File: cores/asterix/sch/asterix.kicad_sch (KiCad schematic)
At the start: 1 part

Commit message: sound and pcm done! wip objects
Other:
- sheet colmix ports: added ~{SYSRES}; removed ~{RESET}
- sheet pcm ports: added ~{SYSRES}; removed ~{RESET}
- sheet scroll ports: added ~{SYSRES}; removed ~{RESET}
- sheet sound ports: added PCMCLK, PCM~{CS}, STBI, ~{SYSRES}; removed SC~{CS}, SH2, SO~{CLK}, S~{CLK}, ~{RESET}
- note added: "OK"
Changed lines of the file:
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@@
-    (stroke (width 0) (type default))
-  )
-  (wire (pts (xy 203.2 57.15) (xy 219.71 57.15))
     (stroke (width 0) (type default))
   )
@@
     (stroke (width 0) (type default))
   )
-  (wire (pts (xy 219.71 54.61) (xy 203.2 54.61))
-    (stroke (width 0) (type default))
-  )
   (wire (pts (xy 148.59 92.71) (xy 165.1 92.71))
     (stroke (width 0) (type default))
@@
     (stroke (width 0) (type default))
   )
-  (wire (pts (xy 203.2 59.69) (xy 219.71 59.69))
+  (wire (pts (xy 203.2 54.61) (xy 219.71 54.61))
     (stroke (width 0) (type default))
   )
@@
   )
   (wire (pts (xy 39.37 107.95) (xy 50.8 107.95))
+    (stroke (width 0) (type default))
+  )
+  (wire (pts (xy 148.59 44.45) (xy 165.1 44.45))
     (stroke (width 0) (type default))
   )
@@
     )
   )
+  (text "OK" (at 184.15 109.22 0)
+    (effects (font (size 1.27 1.27)) (justify left bottom))
+  )
   (text "VSS" (at 39.37 100.33 0)
     (effects (font (size 1.27 1.27)) (justify left bottom))
   )
+  (text "OK" (at 176.53 52.07 0)
+    (effects (font (size 1.27 1.27)) (justify left bottom))
+  )
   (text "VSS" (at 97.79 102.87 0)
     (effects (font (size 1.27 1.27)) (justify left bottom))
@@
     (effects (font (size 1.27 1.27)) (justify left bottom))
   )
-  (label "SC~{CS}" (at 219.71 39.37 180) (fields_autoplaced)
+  (label "PCM~{CS}" (at 219.71 39.37 180) (fields_autoplaced)
     (effects (font (size 1.27 1.27)) (justify right bottom))
   )
@@
     (effects (font (size 1.27 1.27)) (justify right bottom))
   )
+  (label "SH1" (at 148.59 44.45 0) (fields_autoplaced)
+    (effects (font (size 1.27 1.27)) (justify left bottom))
+  )
   (label "COIN_1" (at 39.37 118.11 0) (fields_autoplaced)
     (effects (font (size 1.27 1.27)) (justify left bottom))
@@
     (effects (font (size 1.27 1.27)) (justify left bottom))
   )
-  (label "~{RESET}" (at 311.15 207.01 0) (fields_autoplaced)
+  (label "~{SYSRES}" (at 311.15 207.01 0) (fields_autoplaced)
     (effects (font (size 1.27 1.27)) (justify left bottom))
   )
@@
     (effects (font (size 1.27 1.27)) (justify left bottom))
   )
-  (label "~{RESET}" (at 148.59 41.91 0) (fields_autoplaced)
+  (label "~{SYSRES}" (at 148.59 41.91 0) (fields_autoplaced)
     (effects (font (size 1.27 1.27)) (justify left bottom))
   )
@@
     (effects (font (size 1.27 1.27)) (justify right bottom))
   )
-  (label "SH1" (at 219.71 44.45 180) (fields_autoplaced)
+  (label "STBI" (at 219.71 44.45 180) (fields_autoplaced)
     (effects (font (size 1.27 1.27)) (justify right bottom))
   )
@@
     (effects (font (size 1.27 1.27)) (justify right bottom))
   )
-  (label "~{RESET}" (at 382.27 130.81 180) (fields_autoplaced)
+  (label "~{SYSRES}" (at 382.27 130.81 180) (fields_autoplaced)
     (effects (font (size 1.27 1.27)) (justify right bottom))
   )
@@
     (effects (font (size 1.27 1.27)) (justify left bottom))
   )
-  (label "~{RESET}" (at 148.59 115.57 0) (fields_autoplaced)
+  (label "~{SYSRES}" (at 148.59 115.57 0) (fields_autoplaced)
     (effects (font (size 1.27 1.27)) (justify left bottom))
   )
@@
     (effects (font (size 1.27 1.27)) (justify left bottom))
   )
-  (label "SO~{CLK}" (at 219.71 54.61 180) (fields_autoplaced)
-    (effects (font (size 1.27 1.27)) (justify right bottom))
-  )
   (label "IOCS" (at 148.59 189.23 0) (fields_autoplaced)
     (effects (font (size 1.27 1.27)) (justify left bottom))
@@
     (effects (font (size 1.27 1.27)) (justify right bottom))
   )
+  (label "PCMCLK" (at 148.59 118.11 0) (fields_autoplaced)
+    (effects (font (size 1.27 1.27)) (justify left bottom))
+  )
   (label "2P_BTN_4" (at 97.79 140.97 180) (fields_autoplaced)
     (effects (font (size 1.27 1.27)) (justify right bottom))
@@
     (effects (font (size 1.27 1.27)) (justify left bottom))
   )
-  (label "SH2" (at 219.71 46.99 180) (fields_autoplaced)
-    (effects (font (size 1.27 1.27)) (justify right bottom))
-  )
   (label "OBJPXL[8..0]" (at 381 41.91 180) (fields_autoplaced)
     (effects (font (size 1.27 1.27)) (justify right bottom))
@@
     (effects (font (size 1.27 1.27)) (justify left bottom))
   )
-  (label "S~{RD}" (at 219.71 59.69 180) (fields_autoplaced)
+  (label "S~{RD}" (at 219.71 54.61 180) (fields_autoplaced)
     (effects (font (size 1.27 1.27)) (justify right bottom))
   )
@@
     (effects (font (size 1.27 1.27)) (justify left bottom))
   )
+  (label "PCMCLK" (at 219.71 46.99 180) (fields_autoplaced)
+    (effects (font (size 1.27 1.27)) (justify right bottom))
+  )
   (label "MAIN_DB[7..0]" (at 300.99 125.73 180) (fields_autoplaced)
     (effects (font (size 1.27 1.27)) (justify right bottom))
@@
     (effects (font (size 1.27 1.27)) (justify left bottom))
   )
-  (label "S~{CLK}" (at 219.71 57.15 180) (fields_autoplaced)
-    (effects (font (size 1.27 1.27)) (justify right bottom))
-  )
   (label "MAIN_A0" (at 300.99 130.81 180) (fields_autoplaced)
     (effects (font (size 1.27 1.27)) (justify right bottom))
@@
   (label "~{HBLANK}" (at 382.27 120.65 180) (fields_autoplaced)
     (effects (font (size 1.27 1.27)) (justify right bottom))
-  )
-  (label "S~{CLK}" (at 148.59 118.11 0) (fields_autoplaced)
-    (effects (font (size 1.27 1.27)) (justify left bottom))
   )
   (label "2P_START" (at 148.59 227.33 0) (fields_autoplaced)
@@
       (effects (font (size 1.27 1.27)) (justify left))
     )
-    (pin "~{RESET}" output (at 365.76 130.81 0)
+    (pin "~{SYSRES}" output (at 365.76 130.81 0)
       (effects (font (size 1.27 1.27)) (justify right))
     )
@@
       (effects (font (size 1.27 1.27)) (justify left))
     )
-    (pin "~{RESET}" input (at 327.66 207.01 180)
+    (pin "~{SYSRES}" input (at 327.66 207.01 180)
       (effects (font (size 1.27 1.27)) (justify left))
     )
@@
       (effects (font (size 1.27 1.27)) (justify left))
     )
-    (pin "~{RESET}" input (at 165.1 115.57 180)
+    (pin "~{SYSRES}" input (at 165.1 115.57 180)
       (effects (font (size 1.27 1.27)) (justify left))
     )
@@
       (effects (font (size 1.27 1.27)) (justify left top))
     )
-    (pin "SC~{CS}" output (at 203.2 39.37 0)
+    (pin "PCMCLK" output (at 203.2 46.99 0)
+      (effects (font (size 1.27 1.27)) (justify right))
+    )
+    (pin "S~{RD}" output (at 203.2 54.61 0)
+      (effects (font (size 1.27 1.27)) (justify right))
+    )
+    (pin "~{SOUND}" input (at 165.1 39.37 180)
+      (effects (font (size 1.27 1.27)) (justify left))
+    )
+    (pin "SH1" input (at 165.1 44.45 180)
+      (effects (font (size 1.27 1.27)) (justify left))
+    )
+    (pin "~{SYSRES}" input (at 165.1 41.91 180)
+      (effects (font (size 1.27 1.27)) (justify left))
+    )
+    (pin "SND_A[15..0]" output (at 203.2 52.07 0)
+      (effects (font (size 1.27 1.27)) (justify right))
+    )
+    (pin "SND_D[7..0]" tri_state (at 203.2 49.53 0)
       (effects (font (size 1.27 1.27)) (justify right))
     )
@@
       (effects (font (size 1.27 1.27)) (justify right))
     )
-    (pin "SH1" output (at 203.2 44.45 0)
-      (effects (font (size 1.27 1.27)) (justify right))
-    )
-    (pin "SH2" output (at 203.2 46.99 0)
-      (effects (font (size 1.27 1.27)) (justify right))
-    )
-    (pin "SND_D[7..0]" tri_state (at 203.2 49.53 0)
-      (effects (font (size 1.27 1.27)) (justify right))
-    )
-    (pin "SND_A[15..0]" output (at 203.2 52.07 0)
-      (effects (font (size 1.27 1.27)) (justify right))
-    )
-    (pin "~{SOUND}" input (at 165.1 39.37 180)
-      (effects (font (size 1.27 1.27)) (justify left))
-    )
-    (pin "~{RESET}" input (at 165.1 41.91 180)
-      (effects (font (size 1.27 1.27)) (justify left))
-    )
-    (pin "S~{CLK}" output (at 203.2 57.15 0)
-      (effects (font (size 1.27 1.27)) (justify right))
-    )
-    (pin "S~{RD}" output (at 203.2 59.69 0)
-      (effects (font (size 1.27 1.27)) (justify right))
-    )
-    (pin "SO~{CLK}" output (at 203.2 54.61 0)
-      (effects (font (size 1.27 1.27)) (justify right))
-    )
+    (pin "STBI" output (at 203.2 44.45 0)
+      (effects (font (size 1.27 1.27)) (justify right))
+    )
+    (pin "PCM~{CS}" output (at 203.2 39.37 0)
+      (effects (font (size 1.27 1.27)) (justify right))
+    )

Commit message: wip obj asterix
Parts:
- gave numbers to parts that had none: 1
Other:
- sheet pcm ports: added MAIN_A1, MAIN_D[7..0], PCMCLK, PCM~{CS}, STBI; removed MAIN_A0, MAIN_DB[7..0], SC~{CS}, SH2, SO~{CLK}, S~{CLK}
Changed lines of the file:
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@@
     (stroke (width 0) (type default))
   )
-  (wire (pts (xy 148.59 123.19) (xy 165.1 123.19))
+  (wire (pts (xy 148.59 100.33) (xy 165.1 100.33))
     (stroke (width 0) (type default))
   )
@@
     (stroke (width 0) (type default))
   )
-  (wire (pts (xy 148.59 120.65) (xy 165.1 120.65))
-    (stroke (width 0) (type default))
-  )
   (wire (pts (xy 92.71 81.28) (xy 92.71 83.82))
     (stroke (width 0) (type default))
@@
     (stroke (width 0) (type default))
   )
-  (wire (pts (xy 148.59 100.33) (xy 165.1 100.33))
+  (wire (pts (xy 219.71 102.87) (xy 203.2 102.87))
     (stroke (width 0) (type default))
   )
@@
     (effects (font (size 1.27 1.27)) (justify right bottom))
   )
-  (label "SC~{CS}" (at 148.59 120.65 0) (fields_autoplaced)
-    (effects (font (size 1.27 1.27)) (justify left bottom))
-  )
   (label "~{VSYNC}" (at 311.15 44.45 0) (fields_autoplaced)
     (effects (font (size 1.27 1.27)) (justify left bottom))
@@
     (effects (font (size 1.27 1.27)) (justify left bottom))
   )
-  (label "SH1" (at 148.59 100.33 0) (fields_autoplaced)
-    (effects (font (size 1.27 1.27)) (justify left bottom))
+  (label "SH1" (at 219.71 102.87 180) (fields_autoplaced)
+    (effects (font (size 1.27 1.27)) (justify right bottom))
   )
   (label "1P_DOWN" (at 148.59 199.39 0) (fields_autoplaced)
@@
     (effects (font (size 1.27 1.27)) (justify right bottom))
   )
-  (label "SH2" (at 148.59 102.87 0) (fields_autoplaced)
+  (label "STBI" (at 148.59 102.87 0) (fields_autoplaced)
     (effects (font (size 1.27 1.27)) (justify left bottom))
   )
@@
     (effects (font (size 1.27 1.27)) (justify left bottom))
   )
-  (label "MAIN_A0" (at 148.59 105.41 0) (fields_autoplaced)
+  (label "MAIN_A1" (at 148.59 105.41 0) (fields_autoplaced)
     (effects (font (size 1.27 1.27)) (justify left bottom))
   )
@@
     (effects (font (size 1.27 1.27)) (justify right bottom))
   )
-  (label "SO~{CLK}" (at 148.59 123.19 0) (fields_autoplaced)
+  (label "PCM~{CS}" (at 148.59 100.33 0) (fields_autoplaced)
     (effects (font (size 1.27 1.27)) (justify left bottom))
   )
@@
   (symbol (lib_id "arcade:JAMMA_CONN") (at 54.61 78.74 0) (unit 1)
     (in_bom yes) (on_board yes) (dnp no)
-    (property "Reference" "JM?" (at 68.58 88.9 0)
+    (property "Reference" "JM1" (at 68.58 88.9 0)
       (effects (font (size 3.5052 3.5052)))
     )
@@
       (project "asterix"
         (path "/0011ec10-82c4-4039-b424-337480f568e8"
-          (reference "JM?") (unit 1)
+          (reference "JM1") (unit 1)
         )
       )
@@
     )
   )
-  (sheet (at 165.1 90.17) (size 38.1 35.56) (fields_autoplaced)
+  (sheet (at 165.1 90.17) (size 38.1 30.48) (fields_autoplaced)
     (stroke (width 0.1524) (type solid))
     (fill (color 0 0 0 0.0000))
@@
       (effects (font (size 1.27 1.27)) (justify left bottom))
     )
-    (property "Sheetfile" "pcm.kicad_sch" (at 165.1 126.3146 0)
+    (property "Sheetfile" "pcm.kicad_sch" (at 165.1 121.2346 0)
       (effects (font (size 1.27 1.27)) (justify left top))
     )
-    (pin "SH2" input (at 165.1 102.87 180)
+    (pin "~{MCS}" input (at 165.1 107.95 180)
+      (effects (font (size 1.27 1.27)) (justify left))
+    )
+    (pin "MAIN_A1" input (at 165.1 105.41 180)
+      (effects (font (size 1.27 1.27)) (justify left))
+    )
+    (pin "S~{RD}" input (at 165.1 110.49 180)
+      (effects (font (size 1.27 1.27)) (justify left))
+    )
+    (pin "SH1" output (at 203.2 102.87 0)
+      (effects (font (size 1.27 1.27)) (justify right))
+    )
+    (pin "MAIN_D[7..0]" bidirectional (at 203.2 95.25 0)
+      (effects (font (size 1.27 1.27)) (justify right))
+    )
+    (pin "SND_D[7..0]" bidirectional (at 203.2 92.71 0)
+      (effects (font (size 1.27 1.27)) (justify right))
+    )
+    (pin "PCMCLK" input (at 165.1 118.11 180)
       (effects (font (size 1.27 1.27)) (justify left))
     )
@@
       (effects (font (size 1.27 1.27)) (justify left))
     )
-    (pin "SH1" input (at 165.1 100.33 180)
+    (pin "PCM~{CS}" input (at 165.1 100.33 180)
+      (effects (font (size 1.27 1.27)) (justify left))
+    )
+    (pin "AUX1" input (at 165.1 95.25 180)
+      (effects (font (size 1.27 1.27)) (justify left))
+    )
+    (pin "STBI" input (at 165.1 102.87 180)
+      (effects (font (size 1.27 1.27)) (justify left))
+    )
+    (pin "R{slash}~{W}" input (at 165.1 113.03 180)
+      (effects (font (size 1.27 1.27)) (justify left))
+    )
+    (pin "SND_A[5..0]" input (at 165.1 97.79 180)
       (effects (font (size 1.27 1.27)) (justify left))
     )
@@
       (effects (font (size 1.27 1.27)) (justify left))
     )
-    (pin "MAIN_A0" input (at 165.1 105.41 180)
-      (effects (font (size 1.27 1.27)) (justify left))
-    )
-    (pin "~{MCS}" input (at 165.1 107.95 180)
-      (effects (font (size 1.27 1.27)) (justify left))
-    )
-    (pin "MAIN_DB[7..0]" bidirectional (at 203.2 95.25 0)
-      (effects (font (size 1.27 1.27)) (justify right))
-    )
-    (pin "SND_D[7..0]" bidirectional (at 203.2 92.71 0)
-      (effects (font (size 1.27 1.27)) (justify right))
-    )
-    (pin "S~{RD}" input (at 165.1 110.49 180)
-      (effects (font (size 1.27 1.27)) (justify left))
-    )
-    (pin "R{slash}~{W}" input (at 165.1 113.03 180)
-      (effects (font (size 1.27 1.27)) (justify left))
-    )
-    (pin "SND_A[5..0]" input (at 165.1 97.79 180)
-      (effects (font (size 1.27 1.27)) (justify left))
-    )
-    (pin "AUX1" input (at 165.1 95.25 180)
-      (effects (font (size 1.27 1.27)) (justify left))
-    )
-    (pin "S~{CLK}" input (at 165.1 118.11 180)
-      (effects (font (size 1.27 1.27)) (justify left))
-    )
-    (pin "SC~{CS}" input (at 165.1 120.65 180)
-      (effects (font (size 1.27 1.27)) (justify left))
-    )
     (pin "SPEAKER(+)" output (at 203.2 97.79 0)
       (effects (font (size 1.27 1.27)) (justify right))
@@
       (effects (font (size 1.27 1.27)) (justify right))
     )
-    (pin "SO~{CLK}" input (at 165.1 123.19 180)
-      (effects (font (size 1.27 1.27)) (justify left))
-    )
     (instances

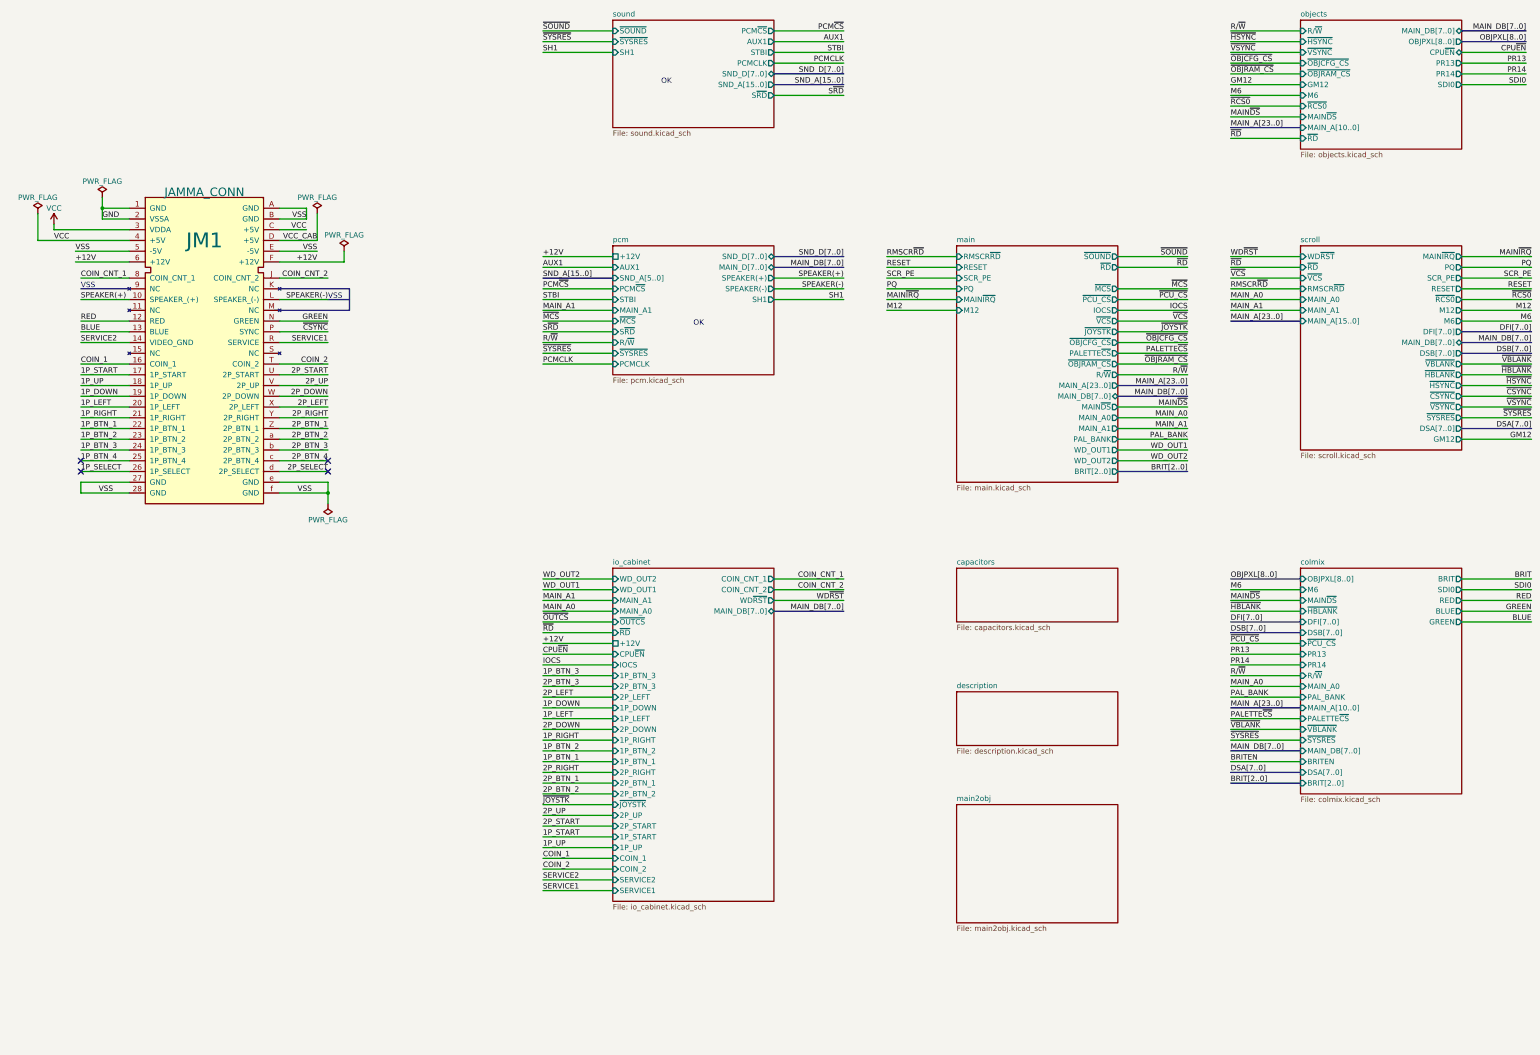
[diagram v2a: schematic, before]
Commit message: objects done. wip of main, sch asterix
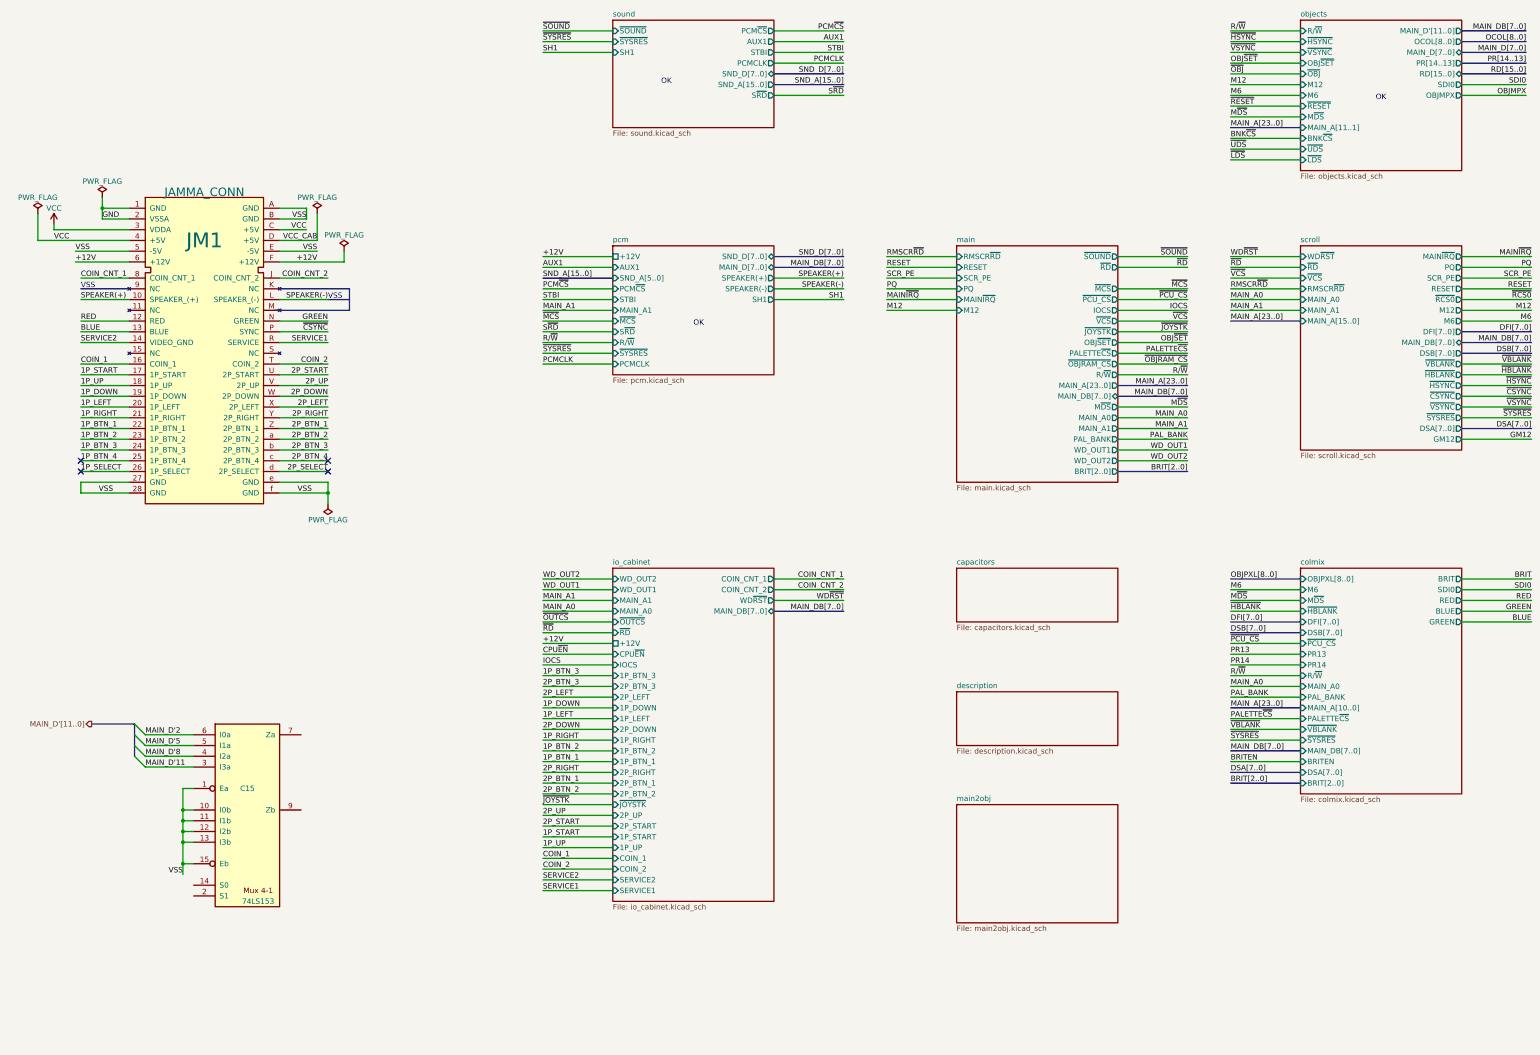
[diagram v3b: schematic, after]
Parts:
- added C15: 74LS153, symbol jt74:74LS153
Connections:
- net VSS: now also C15.1 (Ea), C15.10 (I0b), C15.11 (I1b), C15.12 (I2b), C15.13 (I3b), C15.15 (Eb)
- new net MAIN_D'11: C15.3 (I3a)
- new net MAIN_D'2: C15.6 (I0a)
- new net MAIN_D'5: C15.5 (I1a)
- new net MAIN_D'8: C15.4 (I2a)
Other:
- sheet colmix ports: added M~{DS}; removed MAIN~{DS}
- sheet main ports: added M~{DS}, OBJ~{SET}; removed MAIN~{DS}, ~{OBJCFG_CS}
- sheet objects ports: added BNK~{CS}, M12, MAIN_A[11..1], MAIN_D'[11..0], MAIN_D[7..0], M~{DS}, OBJMPX, OBJ~{SET}, OCOL[8..0], PR[14..13], RD[15..0], ~{LDS}, ~{OBJ}, ~{RESET}, ~{UDS}; removed CPU~{EN}, GM12, MAIN_A[10..0], MAIN_DB[7..0], MAIN~{DS}, OBJPXL[8..0], PR13, PR14, ~{OBJCFG_CS}, ~{OBJRAM_CS}, ~{RCS0}, ~{RD}
